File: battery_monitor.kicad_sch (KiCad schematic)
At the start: 4 parts, among them U1 INA233, U5 ISO1640DBR

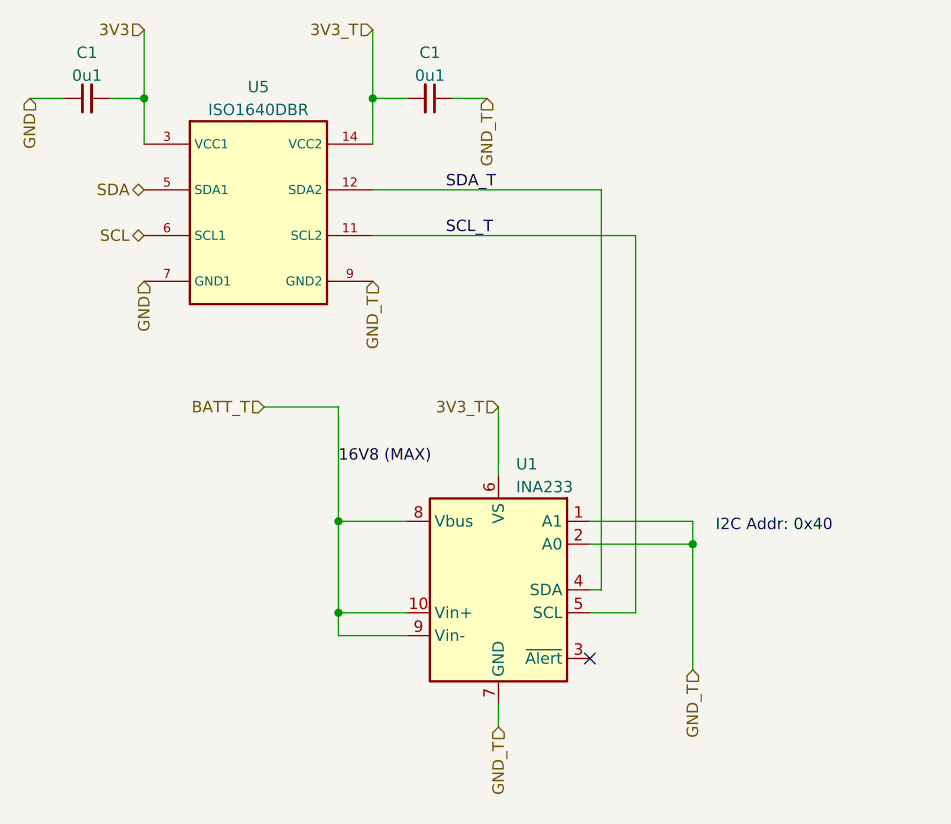
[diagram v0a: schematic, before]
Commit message: Add shunt capacitor for INA233
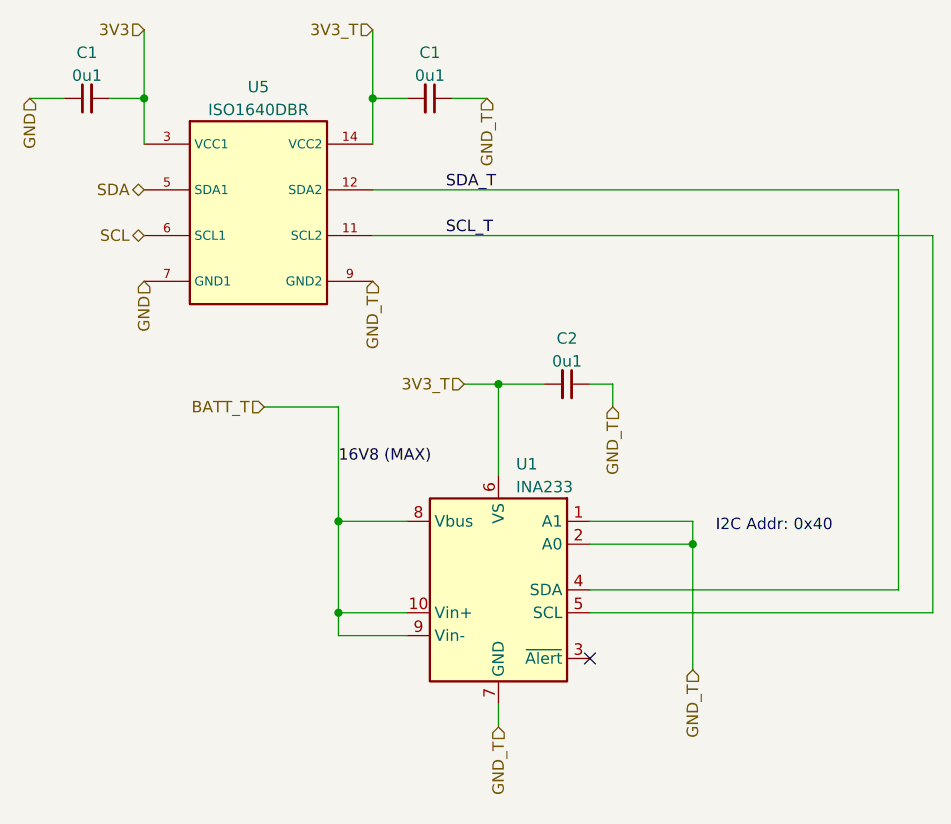
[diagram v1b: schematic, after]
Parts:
- added C2: 0u1, Capacitor_SMD:C_0603_1608Metric_Pad1.08x0.95mm_HandSolder, symbol Device:C_Small
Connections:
- net 3V3_T: now also C2.2
- net GND_T: now also C2.1
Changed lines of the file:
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@@
 (kicad_sch (version 20230121) (generator eeschema)
   (paper "A4")
+  (junction (at 72.39 54.61) (diameter 0) (color 0 0 0 0)
+  )
   (junction (at 54.61 80.01) (diameter 0) (color 0 0 0 0)
   )
@@
   )
   (no_connect (at 82.55 85.09))
-  (wire (pts (xy 82.55 80.01) (xy 87.63 80.01))
-    (stroke (width 0) (type default))
-  )
-  (wire (pts (xy 58.42 38.1) (xy 87.63 38.1))
-    (stroke (width 0) (type default))
-  )
-  (wire (pts (xy 83.82 77.47) (xy 82.55 77.47))
-    (stroke (width 0) (type default))
-  )
-  (wire (pts (xy 58.42 33.02) (xy 83.82 33.02))
+  (wire (pts (xy 82.55 80.01) (xy 120.65 80.01))
+    (stroke (width 0) (type default))
+  )
+  (wire (pts (xy 58.42 38.1) (xy 120.65 38.1))
+    (stroke (width 0) (type default))
+  )
+  (wire (pts (xy 116.84 77.47) (xy 82.55 77.47))
+    (stroke (width 0) (type default))
+  )
+  (wire (pts (xy 58.42 33.02) (xy 116.84 33.02))
     (stroke (width 0) (type default))
   )
@@
     (stroke (width 0) (type default))
   )
+  (wire (pts (xy 72.39 54.61) (xy 77.47 54.61))
+    (stroke (width 0) (type default))
+  )
   (wire (pts (xy 33.02 15.24) (xy 33.02 22.86))
     (stroke (width 0) (type default))
   )
+  (wire (pts (xy 85.09 54.61) (xy 82.55 54.61))
+    (stroke (width 0) (type default))
+  )
   (wire (pts (xy 62.23 69.85) (xy 54.61 69.85))
     (stroke (width 0) (type default))
@@
     (stroke (width 0) (type default))
   )
-  (wire (pts (xy 87.63 38.1) (xy 87.63 80.01))
+  (wire (pts (xy 120.65 38.1) (xy 120.65 80.01))
     (stroke (width 0) (type default))
   )
@@
     (stroke (width 0) (type default))
   )
+  (wire (pts (xy 72.39 54.61) (xy 72.39 64.77))
+    (stroke (width 0) (type default))
+  )
   (wire (pts (xy 62.23 82.55) (xy 54.61 82.55))
     (stroke (width 0) (type default))
@@
     (stroke (width 0) (type default))
   )
+  (wire (pts (xy 85.09 57.15) (xy 85.09 54.61))
+    (stroke (width 0) (type default))
+  )
   (wire (pts (xy 82.55 69.85) (xy 93.98 69.85))
     (stroke (width 0) (type default))
   )
+  (wire (pts (xy 68.58 54.61) (xy 72.39 54.61))
+    (stroke (width 0) (type default))
+  )
   (wire (pts (xy 62.23 22.86) (xy 58.42 22.86))
     (stroke (width 0) (type default))
@@
     (stroke (width 0) (type default))
   )
-  (wire (pts (xy 83.82 33.02) (xy 83.82 77.47))
+  (wire (pts (xy 116.84 33.02) (xy 116.84 77.47))
     (stroke (width 0) (type default))
   )
   (wire (pts (xy 33.02 22.86) (xy 33.02 27.94))
-    (stroke (width 0) (type default))
-  )
-  (wire (pts (xy 72.39 57.15) (xy 72.39 64.77))
     (stroke (width 0) (type default))
   )
@@
     (effects (font (size 1.27 1.27)) (justify right))
   )
+  (hierarchical_label "GND_T" (shape input) (at 85.09 57.15 270) (fields_autoplaced)
+    (effects (font (size 1.27 1.27)) (justify right))
+  )
   (hierarchical_label "GND_T" (shape input) (at 71.12 22.86 270) (fields_autoplaced)
     (effects (font (size 1.27 1.27)) (justify right))
@@
     (effects (font (size 1.27 1.27)) (justify right))
   )
-  (hierarchical_label "3V3_T" (shape input) (at 72.39 57.15 180) (fields_autoplaced)
+  (hierarchical_label "3V3_T" (shape input) (at 68.58 54.61 180) (fields_autoplaced)
     (effects (font (size 1.27 1.27)) (justify right))
   )
@@
         )
       )
+    )
+  )
+  (symbol (lib_id "Device:C_Small") (at 80.01 54.61 270) (mirror x) (unit 1)
+    (in_bom yes) (on_board yes) (dnp no)
+    (property "Reference" "C2" (at 80.01 49.53 90)
+      (effects (font (size 1.27 1.27)))
+    )
+    (property "Value" "0u1" (at 80.01 52.07 90)
+      (effects (font (size 1.27 1.27)))
+    )
+    (property "Footprint" "Capacitor_SMD:C_0603_1608Metric_Pad1.08x0.95mm_HandSolder" (at 80.01 54.61 0)
+      (effects (font (size 1.27 1.27)) hide)
+    )
+    (property "Datasheet" "~" (at 80.01 54.61 0)
+      (effects (font (size 1.27 1.27)) hide)
+    )
+    (pin "1")
+    (pin "2")
+    (instances
+      (project "battery_monitor"
+        (path "/1fcc1511-5bc9-4c85-8375-68c4eda7e380"
+          (reference "C2") (unit 1)
+        )
+      )
+      (project "crush-main-board"
+        (path "/74b566fe-9d71-4817-95ed-d472d647f8c8"
+          (reference "C1") (unit 1)
+        )
+        (path "/74b566fe-9d71-4817-95ed-d472d647f8c8/bd306228-21c6-4f00-bab7-e02ca2e320ac"
+          (reference "C6") (unit 1)
+        )
+      )

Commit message: Switch to INA232
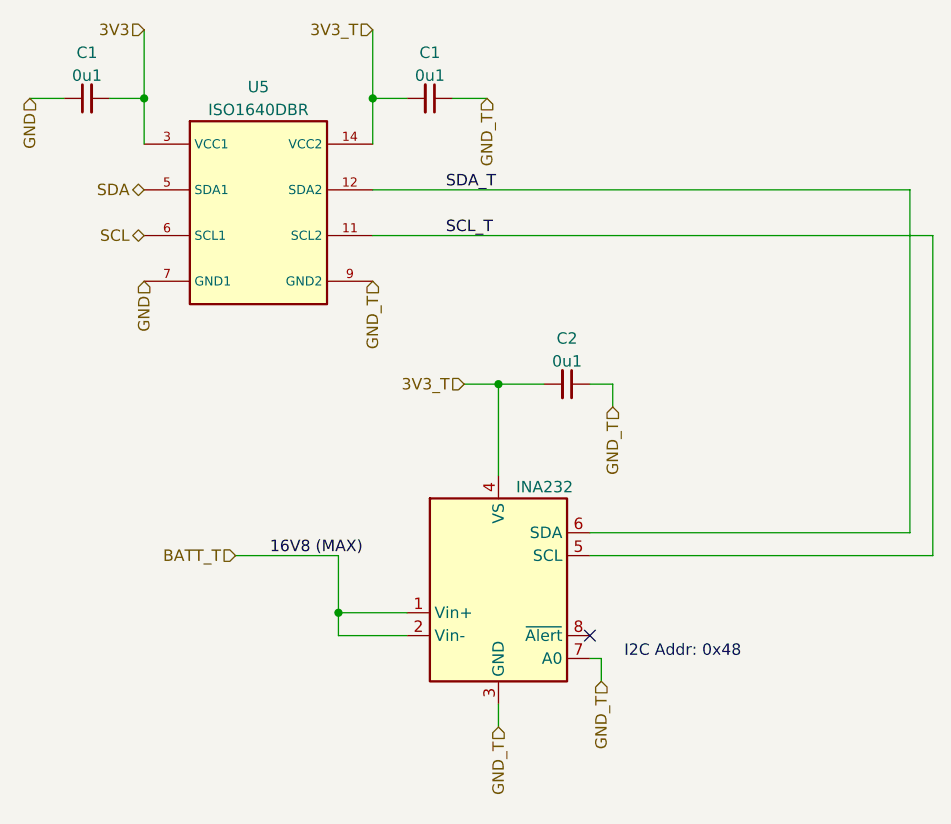
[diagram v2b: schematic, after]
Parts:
- removed U1: INA233, Package_SO:VSSOP-10_3x3mm_P0.5mm, symbol Sensor_Energy:INA233
- added INA232: ~, Package_TO_SOT_SMD:SOT-23-8_Handsoldering, symbol Crush_MainBoard_Symbols:INA232
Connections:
- net 3V3_T: now also INA232.4 (VS)
- net BATT_T: now also INA232.1 (Vin+), INA232.2 (Vin-)
- net GND_T: now also INA232.3 (GND), INA232.7 (A0)
- net SCL_T: now also INA232.5 (SCL)
- net SDA_T: now also INA232.6 (SDA)
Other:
- note added: "I2C Addr: 0x48"
- note removed: "I2C Addr: 0x40"
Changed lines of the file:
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@@
   (junction (at 33.02 22.86) (diameter 0) (color 0 0 0 0)
   )
-  (junction (at 93.98 72.39) (diameter 0) (color 0 0 0 0)
-  )
-  (junction (at 54.61 69.85) (diameter 0) (color 0 0 0 0)
-  )
-  (no_connect (at 82.55 85.09))
-  (wire (pts (xy 82.55 80.01) (xy 120.65 80.01))
-    (stroke (width 0) (type default))
-  )
+  (no_connect (at 82.55 82.55))
   (wire (pts (xy 58.42 38.1) (xy 120.65 38.1))
     (stroke (width 0) (type default))
   )
-  (wire (pts (xy 116.84 77.47) (xy 82.55 77.47))
-    (stroke (width 0) (type default))
-  )
-  (wire (pts (xy 58.42 33.02) (xy 116.84 33.02))
+  (wire (pts (xy 58.42 33.02) (xy 118.11 33.02))
+    (stroke (width 0) (type default))
+  )
+  (wire (pts (xy 82.55 73.66) (xy 120.65 73.66))
     (stroke (width 0) (type default))
   )
@@
     (stroke (width 0) (type default))
   )
-  (wire (pts (xy 62.23 69.85) (xy 54.61 69.85))
-    (stroke (width 0) (type default))
-  )
-  (wire (pts (xy 54.61 69.85) (xy 54.61 57.15))
-    (stroke (width 0) (type default))
-  )
-  (wire (pts (xy 120.65 38.1) (xy 120.65 80.01))
-    (stroke (width 0) (type default))
-  )
-  (wire (pts (xy 93.98 69.85) (xy 93.98 72.39))
+  (wire (pts (xy 120.65 38.1) (xy 120.65 73.66))
     (stroke (width 0) (type default))
   )
@@
     (stroke (width 0) (type default))
   )
-  (wire (pts (xy 82.55 72.39) (xy 93.98 72.39))
+  (wire (pts (xy 83.82 85.09) (xy 83.82 87.63))
     (stroke (width 0) (type default))
   )
@@
     (stroke (width 0) (type default))
   )
-  (wire (pts (xy 82.55 69.85) (xy 93.98 69.85))
-    (stroke (width 0) (type default))
-  )
   (wire (pts (xy 68.58 54.61) (xy 72.39 54.61))
     (stroke (width 0) (type default))
@@
     (stroke (width 0) (type default))
   )
-  (wire (pts (xy 93.98 72.39) (xy 93.98 86.36))
-    (stroke (width 0) (type default))
-  )
   (wire (pts (xy 72.39 90.17) (xy 72.39 92.71))
     (stroke (width 0) (type default))
   )
-  (wire (pts (xy 46.355 57.15) (xy 54.61 57.15))
-    (stroke (width 0) (type default))
-  )
-  (wire (pts (xy 116.84 33.02) (xy 116.84 77.47))
+  (wire (pts (xy 43.18 73.66) (xy 54.61 73.66))
+    (stroke (width 0) (type default))
+  )
+  (wire (pts (xy 118.11 33.02) (xy 118.11 71.12))
+    (stroke (width 0) (type default))
+  )
+  (wire (pts (xy 82.55 71.12) (xy 118.11 71.12))
     (stroke (width 0) (type default))
   )
@@
     (stroke (width 0) (type default))
   )
-  (wire (pts (xy 54.61 69.85) (xy 54.61 80.01))
+  (wire (pts (xy 54.61 73.66) (xy 54.61 80.01))
+    (stroke (width 0) (type default))
+  )
+  (wire (pts (xy 82.55 85.09) (xy 83.82 85.09))
     (stroke (width 0) (type default))
   )
@@
     (stroke (width 0) (type default))
   )
-  (text "I2C Addr: 0x40" (at 96.52 71.12 0)
+  (text "I2C Addr: 0x48" (at 86.36 85.09 0)
     (effects (font (size 1.27 1.27)) (justify left bottom))
   )
@@
     (effects (font (size 1.27 1.27)) (justify left bottom))
   )
-  (label "16V8 (MAX)" (at 54.61 63.5 0) (fields_autoplaced)
+  (label "16V8 (MAX)" (at 46.99 73.66 0) (fields_autoplaced)
     (effects (font (size 1.27 1.27)) (justify left bottom))
   )
@@
     (effects (font (size 1.27 1.27)) (justify right))
   )
-  (hierarchical_label "BATT_T" (shape input) (at 46.355 57.15 180) (fields_autoplaced)
+  (hierarchical_label "BATT_T" (shape input) (at 43.18 73.66 180) (fields_autoplaced)
     (effects (font (size 1.27 1.27)) (justify right))
   )
@@
     (effects (font (size 1.27 1.27)) (justify right))
   )
+  (hierarchical_label "GND_T" (shape input) (at 83.82 87.63 270) (fields_autoplaced)
+    (effects (font (size 1.27 1.27)) (justify right))
+  )
   (hierarchical_label "SDA" (shape bidirectional) (at 33.02 33.02 180) (fields_autoplaced)
     (effects (font (size 1.27 1.27)) (justify right))
@@
   )
   (hierarchical_label "3V3" (shape input) (at 33.02 15.24 180) (fields_autoplaced)
-    (effects (font (size 1.27 1.27)) (justify right))
-  )
-  (hierarchical_label "GND_T" (shape input) (at 93.98 86.36 270) (fields_autoplaced)
     (effects (font (size 1.27 1.27)) (justify right))
   )
@@
     )
   )
-  (symbol (lib_id "Sensor_Energy:INA233") (at 72.39 77.47 0) (unit 1)
-    (in_bom yes) (on_board yes) (dnp no)
-    (property "Reference" "U1" (at 74.3459 63.5 0)
+  (symbol (lib_id "Crush_MainBoard_Symbols:INA232") (at 72.39 76.2 0) (unit 1)
+    (in_bom yes) (on_board yes) (dnp no) (fields_autoplaced)
+    (property "Reference" "INA232" (at 74.3459 66.04 0)
       (effects (font (size 1.27 1.27)) (justify left))
     )
-    (property "Value" "INA233" (at 74.3459 66.04 0)
-      (effects (font (size 1.27 1.27)) (justify left))
-    )
-    (property "Footprint" "Package_SO:VSSOP-10_3x3mm_P0.5mm" (at 92.71 88.9 0)
-      (effects (font (size 1.27 1.27)) hide)
-    )
-    (property "Datasheet" "https://www.ti.com/lit/ds/symlink/ina233.pdf" (at 81.28 80.01 0)
+    (property "Value" "~" (at 72.39 77.47 0)
+      (effects (font (size 1.27 1.27)))
+    )
+    (property "Footprint" "Package_TO_SOT_SMD:SOT-23-8_Handsoldering" (at 72.39 44.45 0)
+      (effects (font (size 1.27 1.27)) hide)
+    )
+    (property "Datasheet" "https://www.ti.com/lit/ds/symlink/ina232.pdf" (at 72.39 49.53 0)
       (effects (font (size 1.27 1.27)) hide)
     )
     (pin "1")
-    (pin "10")
     (pin "2")
     (pin "3")
@@
     (pin "7")
     (pin "8")
-    (pin "9")
-    (instances
-      (project "battery_monitor"
-        (path "/1fcc1511-5bc9-4c85-8375-68c4eda7e380"
-          (reference "U1") (unit 1)
-        )
-      )
-      (project "crush-power-board"
-        (path "/530b9f5d-4c5f-47a4-a889-3cce870d311f"
-          (reference "U5") (unit 1)
-        )
-      )
-      (project "crush-main-board"
-        (path "/74b566fe-9d71-4817-95ed-d472d647f8c8/bd306228-21c6-4f00-bab7-e02ca2e320ac"
-          (reference "U1") (unit 1)
-        )
-      )
+    (instances
+      (project "crush-main-board"
+        (path "/74b566fe-9d71-4817-95ed-d472d647f8c8/bd306228-21c6-4f00-bab7-e02ca2e320ac"
+          (reference "INA232") (unit 1)
+        )
+      )

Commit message: Updated reference for current monitoring chip
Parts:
- renumbered INA232 to INA232B
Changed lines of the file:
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@@
   (symbol (lib_id "Crush_MainBoard_Symbols:INA232") (at 72.39 76.2 0) (unit 1)
     (in_bom yes) (on_board yes) (dnp no) (fields_autoplaced)
-    (property "Reference" "INA232" (at 74.3459 66.04 0)
+    (property "Reference" "INA232B" (at 74.5841 64.77 0)
       (effects (font (size 1.27 1.27)) (justify left))
     )
@@
       (project "crush-main-board"
         (path "/74b566fe-9d71-4817-95ed-d472d647f8c8/bd306228-21c6-4f00-bab7-e02ca2e320ac"
-          (reference "INA232") (unit 1)
+          (reference "INA232B") (unit 1)
         )
       )

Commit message: Start laying out main board
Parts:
- renumbered INA232B to INA232B1
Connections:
- net BATT_T renamed BATT
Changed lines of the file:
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@@
     (effects (font (size 1.27 1.27)) (justify right))
   )
-  (hierarchical_label "BATT_T" (shape input) (at 43.18 73.66 180) (fields_autoplaced)
+  (hierarchical_label "BATT" (shape input) (at 43.18 73.66 180) (fields_autoplaced)
     (effects (font (size 1.27 1.27)) (justify right))
   )
@@
   (symbol (lib_id "Crush_MainBoard_Symbols:INA232") (at 72.39 76.2 0) (unit 1)
     (in_bom yes) (on_board yes) (dnp no) (fields_autoplaced)
-    (property "Reference" "INA232B" (at 74.5841 64.77 0)
+    (property "Reference" "INA232B1" (at 74.5841 64.77 0)
       (effects (font (size 1.27 1.27)) (justify left))
     )
@@
       (project "crush-main-board"
         (path "/74b566fe-9d71-4817-95ed-d472d647f8c8/bd306228-21c6-4f00-bab7-e02ca2e320ac"
-          (reference "INA232B") (unit 1)
+          (reference "INA232B1") (unit 1)
         )
       )
@@
         )
         (path "/74b566fe-9d71-4817-95ed-d472d647f8c8/bd306228-21c6-4f00-bab7-e02ca2e320ac"
-          (reference "C6") (unit 1)
+          (reference "C7") (unit 1)
         )
       )
